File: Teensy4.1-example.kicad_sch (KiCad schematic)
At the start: 80 parts, among them IC1 MIMXRT1062DVJ6B, J1 Conn_01x11_Male, J2 Conn_01x11_Male, J3 Conn_01x12_Male, J4 Conn_01x11_Male, J5 Conn_01x11_Male, J6 Conn_01x03_Male, J7 Conn_01x03_Male, P2 D26, Q1 Q_PMOS_GDS_DMP3125L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

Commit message: Migrate to kicad8
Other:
- moved on the sheet: C1, C10, C11, C12, C13, C14, C15, C16, C17, C18, C19, C2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

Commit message: Schematics changes - Back to use TPD3S014DBVR for USB switch - Add JLC part numbers
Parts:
- removed D2: LED, LED_SMD:LED_0402_1005Metric, symbol Device:LED
- removed R6, R7: 16k, Resistor_SMD:R_0603_1608Metric, symbol Device:R
- removed R8: 1k, Resistor_SMD:R_0402_1005Metric, symbol Device:R
- removed U2: MAX1562, Package_SO:SO-8_3.9x4.9mm_P1.27mm, symbol MIMXRT1062DVJ6B:MAX1562
- added C27: 100uF, Capacitor_SMD:C_1206_3216Metric, symbol Device:C
- added U5: TPD3S014DBVR, Package_TO_SOT_SMD:SOT-23-6, symbol Power_Protection:TPD3S014
- C1, C10, C13, C17, C18, C2, C23, C25, C4, C8: LCSC (none) -> C106216
- C11, C14, C9: LCSC (none) -> C2167686
- C12, C15, C24, C26, C6: LCSC (none) -> C107368
- C16, C5: LCSC (none) -> C163173
- C19, C20: LCSC (none) -> C1634
- C21, C22: LCSC (none) -> C430713
- C3, C7: LCSC (none) -> C100082
- D1, Di3: LCSC (none) -> C3040626
- D3, D4: LCSC (none) -> C264407
- D5: LCSC (none) -> C266596
- F1: LCSC (none) -> C5220829
- FB1, FB2: LCSC (none) -> C454098
- IC1: LCSC (none) -> C3216699
- L1: LCSC (none) -> C86090
- NCP692: LCSC (none) -> C145519
- PROG1: LCSC (none) -> C221682
- Q1: LCSC (none) -> C459542
- R1, R2: LCSC (none) -> C105580
- R10, R14: LCSC (none) -> C11702
- R11, R16, R3, R4: LCSC (none) -> C15458
- R12, R13: LCSC (none) -> C23206
- R15: LCSC (none) -> C18679
- R5, R9: LCSC (none) -> C22935
- U3: LCSC (none) -> C5440778
- USB_DFP1, USB_UFP1: LCSC (none) -> C223907
- Y1: value Crystal_GND23 -> 24MHz; LCSC (none) -> C5544458
- Y2: value Crystal -> 32.768kHz; LCSC (none) -> C510776
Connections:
- net +5VD: now also U5.3 (IN)
- net +5VL: now also C27.1, U5.4 (OUT)
- net GND: now also C27.2, U5.2 (GND)
- net USB2_DN: now also U5.5 (D1)
- net USB2_DP: now also U5.6 (D2)
- net at IC1.A7 (GPIO_EMC_40), R16.2: now also U5.1 (EN)
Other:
- moved on the sheet: Di3, R12, R13, R9, USB_DFP1

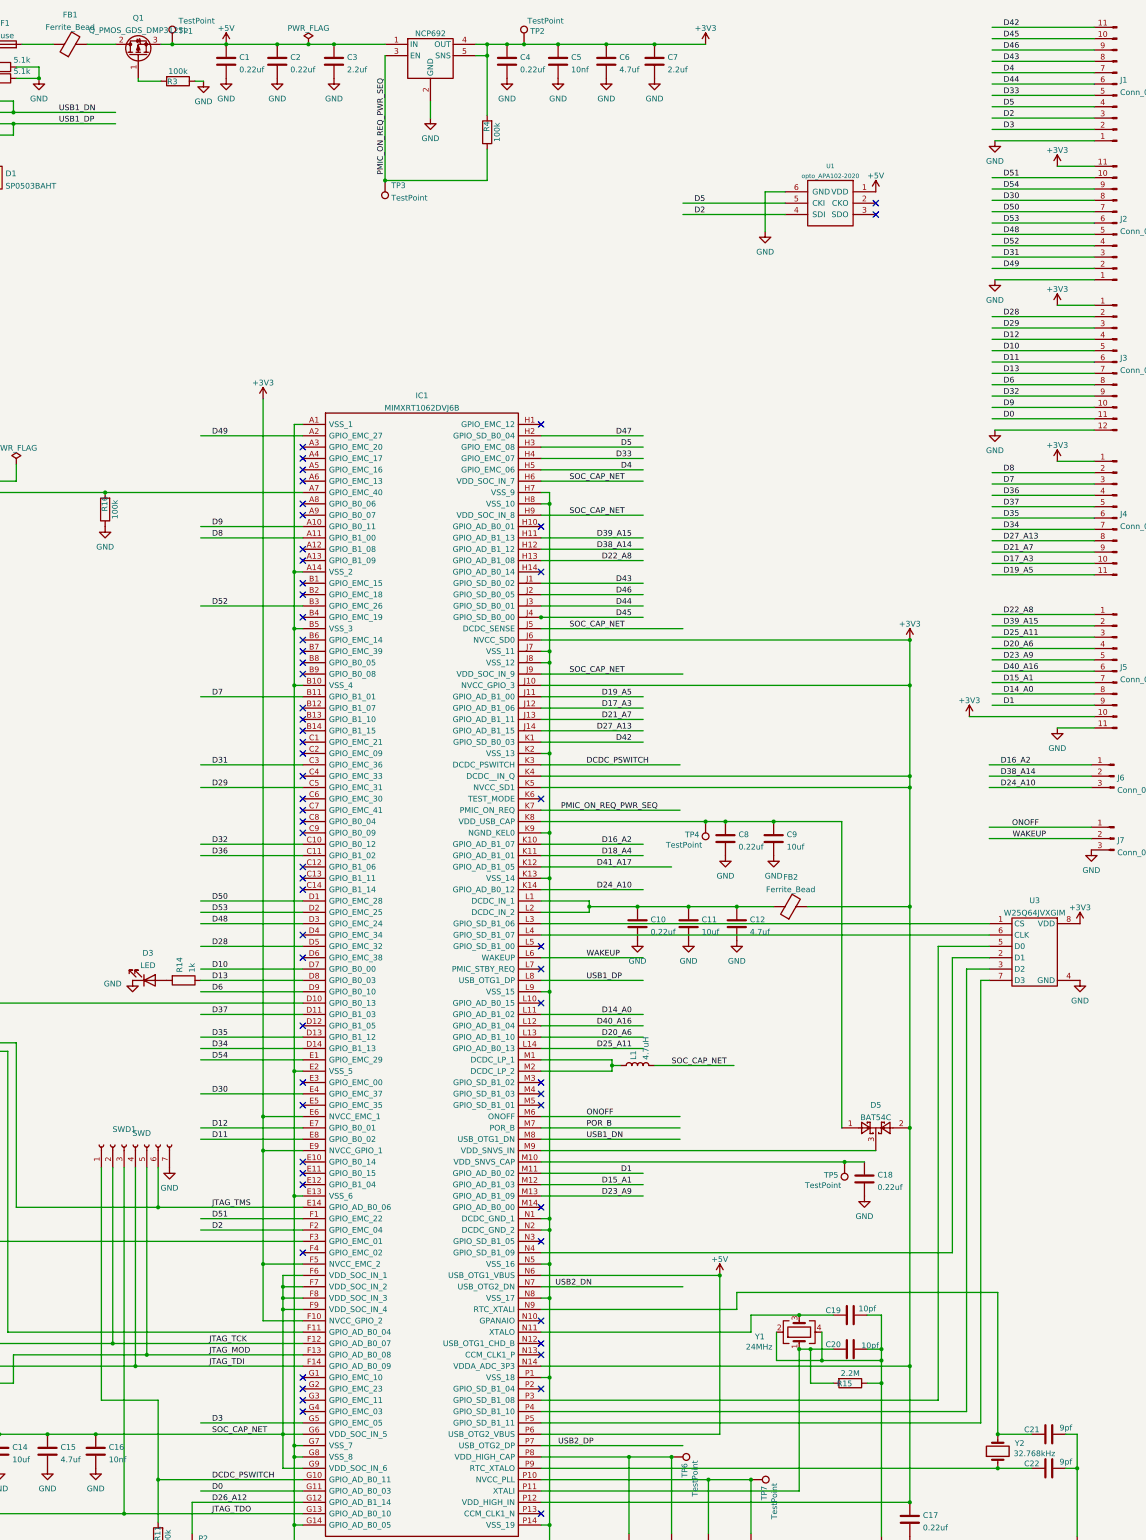
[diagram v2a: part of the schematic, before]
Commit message: Remove the RGB LED
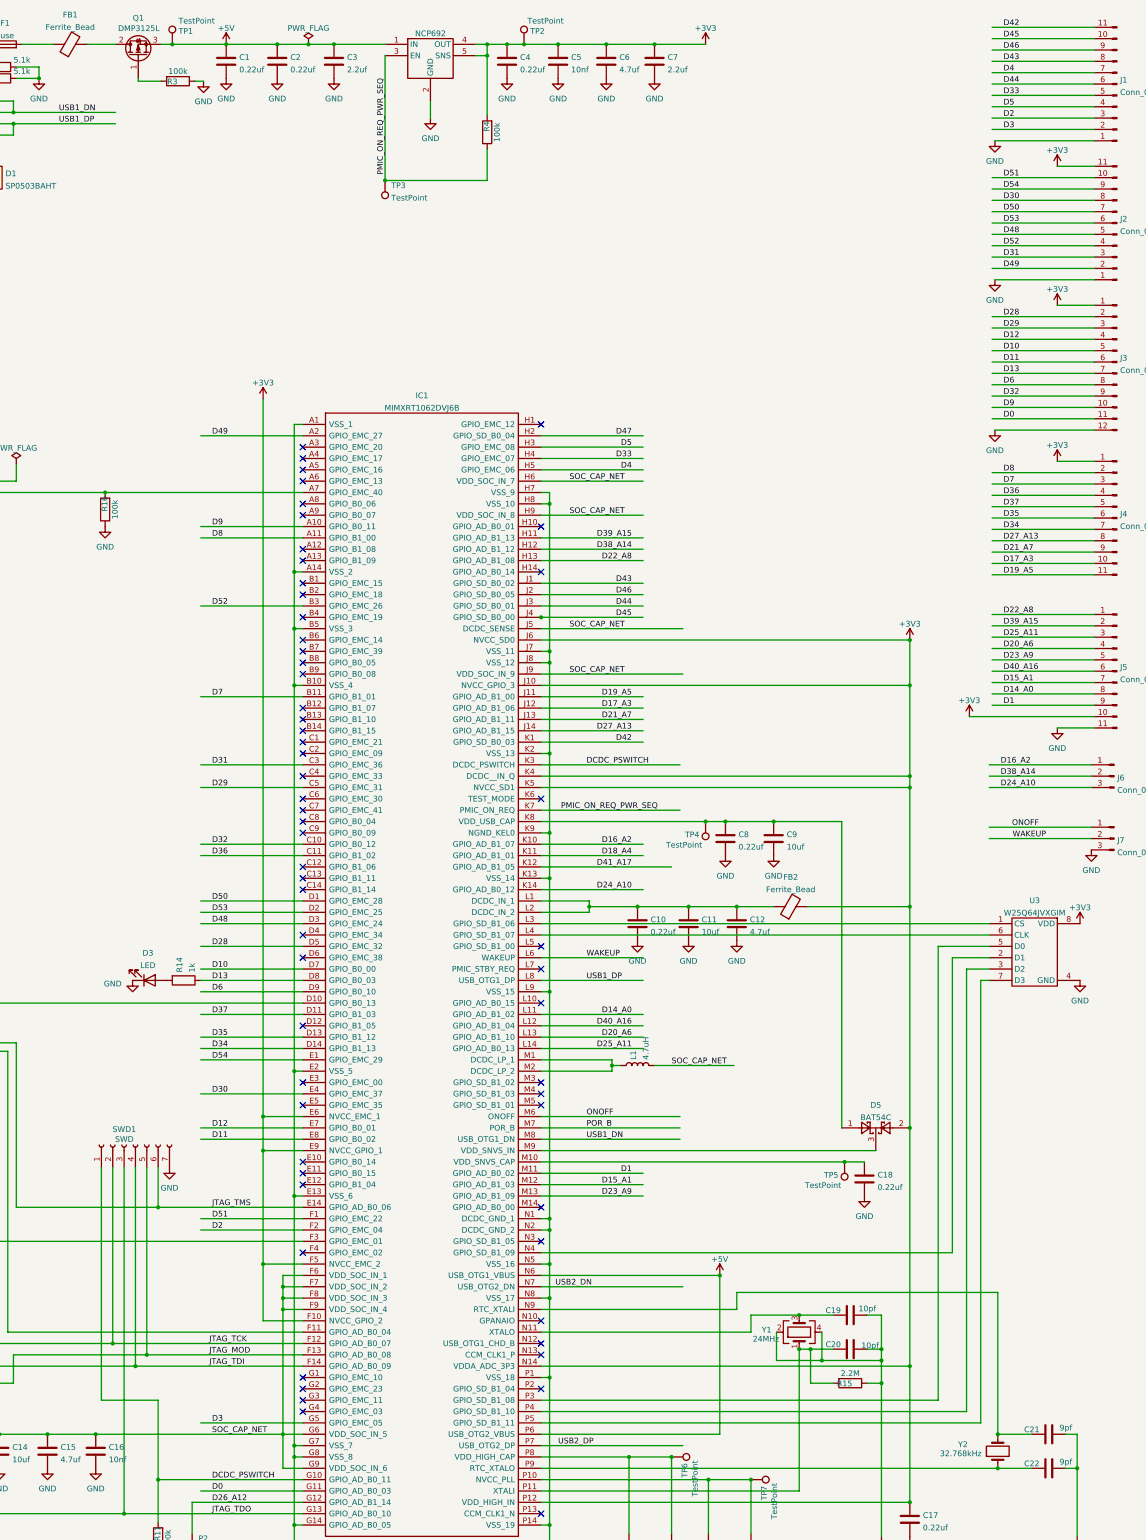
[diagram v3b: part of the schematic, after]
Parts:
- removed U1: opto_APA102-2020, USB-C-Power-tester:APA102-2020, symbol APA102:opto_APA102-2020
- Q1: value Q_PMOS_GDS_DMP3125L -> DMP3125L
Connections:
- no-connect marks 66 -> 64
